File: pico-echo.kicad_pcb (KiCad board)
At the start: 2 copper layers, 22.9 x 50.8 mm, 51 parts, among them J1 USB_C_Receptacle_USB2.0, J2 I2C, J4 Conn_01x16, J5 Conn_01x12, J6 BAT, Q1 BSS83P, SW1 SW_Push, SW2 SW_Push, U1 RP2040, U2 W25Q128JVS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

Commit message: Updated tracks, not finished yet
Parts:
- D2: footprint Capacitor_SMD:C_0603_1608Metric -> LED_SMD:LED_0603_1608Metric
- moved D2 54.9 mm to (138.1, 68.2), turned to 90 degrees
- moved D4 54.3 mm to (126.0, 68.2), turned to -90 degrees
- moved C2 50.7 mm to (131.1, 90.1)
- moved R2 50.7 mm to (131.1, 91.4)
- moved C1 50.7 mm to (136.2, 90.6)
- moved Y1 50.7 mm to (133.9, 90.6)
- moved R5 50.5 mm to (126.1, 71.9)
- moved U1 50.4 mm to (132.0, 97.1)
- moved R7 50.3 mm to (130.8, 74.3), turned to -90 degrees
- moved U4 50.3 mm to (136.8, 84.0)
- moved U2 50.1 mm to (134.7, 106.8)
- moved J1 49.7 mm to (132.0, 68.6)
- moved D1 49.7 mm to (132.9, 78.2)
- moved D5 49.7 mm to (126.7, 84.0)
- moved J2 49.7 mm to (129.2, 111.9)
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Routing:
- net VBUS: track 3.72 -> 27.2 mm, vias 0 -> 2
- net Net-(D3-K): track 0.00 -> 8.36 mm
- net /QSPI_SS: track 0.00 -> 7.81 mm
- net +3V3: track 0.00 -> 6.76 mm
- net Net-(J1-CC1): track 0.00 -> 6.68 mm
- net Net-(J1-CC2): track 0.00 -> 6.21 mm
- net Net-(J1-D--PadA7): track 0.00 -> 4.70 mm
- net Net-(D2-A): track 0.00 -> 4.45 mm
- net Net-(J1-D+-PadA6): track 0.00 -> 3.71 mm
- net Net-(D1-K): track 6.73 -> 9.81 mm
- net Net-(D4-A): track 0.00 -> 2.74 mm
- net Net-(D3-A): track 0.00 -> 2.01 mm
- net Net-(U4-PROG): track 0.00 -> 1.62 mm
- net VBAT: track 4.65 -> 6.23 mm
- net Net-(U3-EN): track 0.00 -> 1.50 mm
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- added copper zone on B.Cu, net GND
- added copper zone on F.Cu, net GND
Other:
- board text added: "10"
- board text added: "11"
- board text added: "12"
- board text added: "13"
- board text added: "24"
- board text added: "25"
- board text added: "3V3"
- board text added: "5"
- board text added: "6"
- board text added: "9"
- board text added: "A0"
- board text added: "A1"
- board text added: "A2"
- board text added: "A3"
- board text added: "BAT"
- board text added: "D4"
- board text added: "EN"
- board text added: "GND"
- board text added: "M0"
- board text added: "M1"
- board text added: "RST"
- board text added: "RX"
- board text added: "SCK"
- board text added: "SCL"
- board text added: "SDA"
- board text added: "TX"
- board text added: "USB"

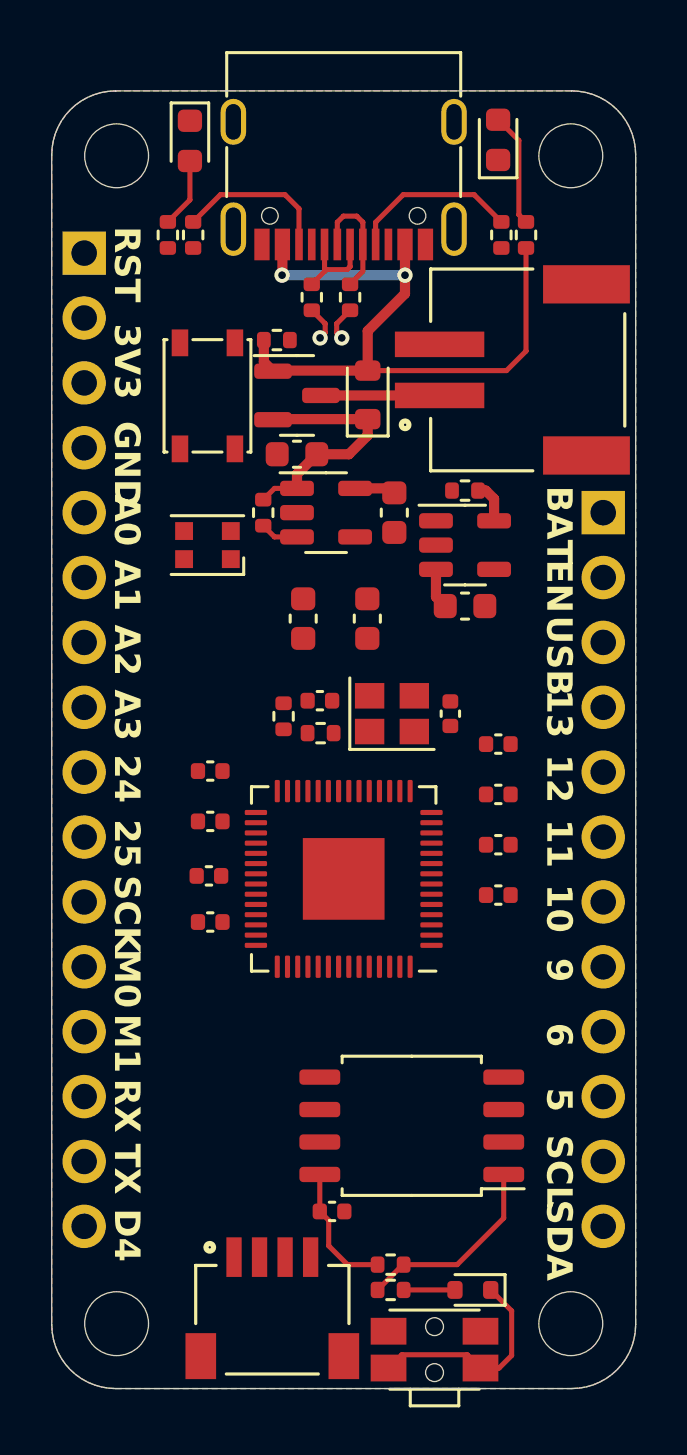
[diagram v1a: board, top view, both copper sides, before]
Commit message: Add SWD conn, change Flash to USON, tracks almost finished
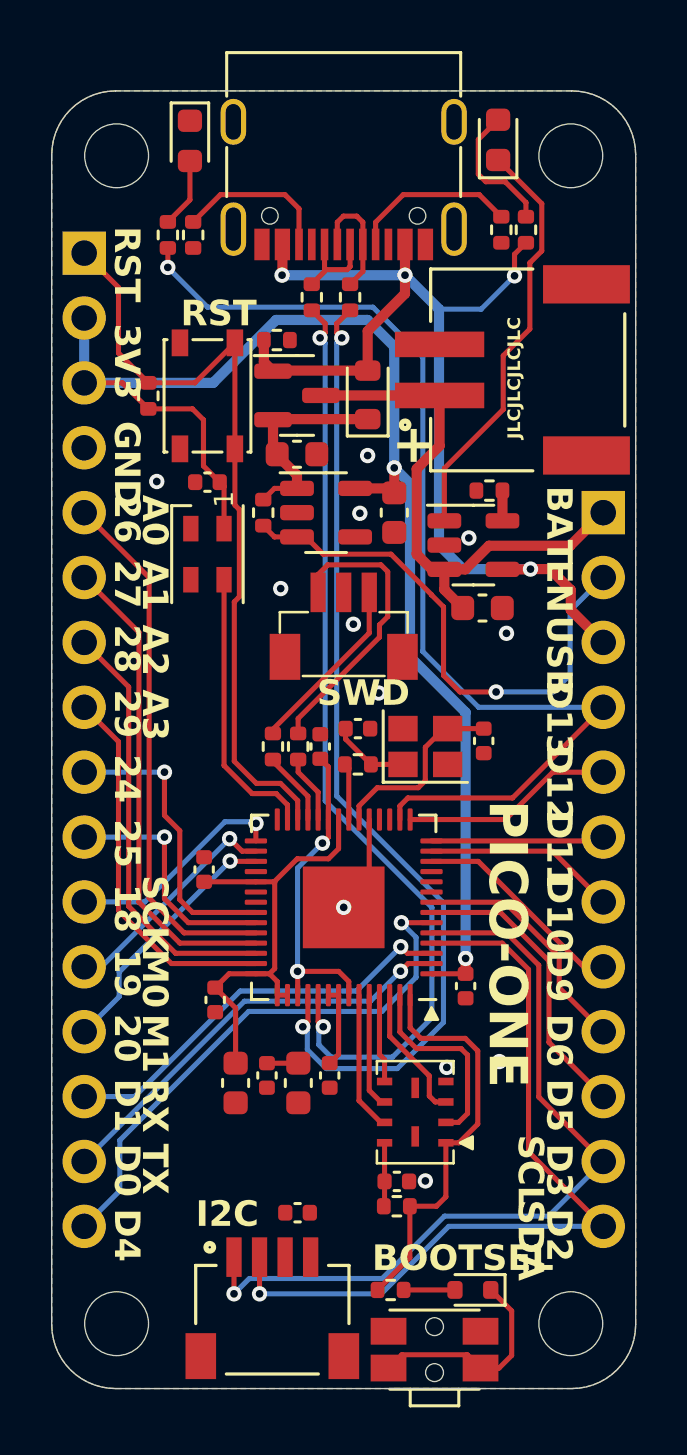
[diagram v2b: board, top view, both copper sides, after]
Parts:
- added J7: PICO Probe, BM03B-SRSS-TBT_LF__SN_:BM03BSRSSTBTLFSN, F.Cu at (132.0, 86.7)
- added R14: 100, Resistor_SMD:R_0402_1005Metric, F.Cu at (130.2, 91.9)
- added R15: 100, Resistor_SMD:R_0402_1005Metric, F.Cu at (129.2, 91.9)
- D5: footprint LED_SMD:LED_WS2812B-2020_PLCC4_2.0x2.0mm -> LED_SMD:LED_SK6805_PLCC4_2.4x2.7mm_P1.3mm
- U2: footprint Package_SO:SOIC-8_5.23x5.23mm_P1.27mm -> SPI-Flash:USON-8-3x4
- moved C9 18.4 mm to (130.2, 105.1), turned to -90 degrees
- moved C6 18.4 mm to (127.8, 105.1), turned to -90 degrees
- moved C7 15.8 mm to (129.0, 104.8), turned to -90 degrees
- moved C13 15.7 mm to (130.2, 110.2)
- moved R1 13.6 mm to (124.4, 78.2), turned to 90 degrees
- moved C12 11.3 mm to (126.7, 81.6), turned to 180 degrees
- moved C11 9.67 mm to (131.5, 104.8), turned to -90 degrees
- moved C8 7.22 mm to (131.1, 91.9), turned to 90 degrees
- moved C10 5.68 mm to (136.8, 101.3), turned to -90 degrees
- moved C15 3.06 mm to (127.0, 101.9), turned to -90 degrees
- moved C16 2.79 mm to (134.1, 109.0)
- moved R3 2.30 mm to (134.1, 109.9)
- moved R2 1.91 mm to (132.6, 92.6)
- moved C2 1.85 mm to (132.6, 91.2)
- moved Y1 1.83 mm to (135.2, 91.9)
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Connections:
- D5 pad 4: /RGB_LED -> /GPIO16
- J2 pad 1: /SCL -> /GPIO3
- J2 pad 2: /SDA -> /GPIO2
- J4 pad 10: unconnected-(J4-Pin_10-Pad10) -> /GPIO25
- J4 pad 11: unconnected-(J4-Pin_11-Pad11) -> /GPIO18
- J4 pad 12: unconnected-(J4-Pin_12-Pad12) -> /GPIO19
- J4 pad 13: unconnected-(J4-Pin_13-Pad13) -> /GPIO20
- J4 pad 14: unconnected-(J4-Pin_14-Pad14) -> /GPIO1
- J4 pad 15: unconnected-(J4-Pin_15-Pad15) -> /GPIO0
- J4 pad 16: unconnected-(J4-Pin_16-Pad16) -> /GPIO4
- J4 pad 3: GND -> +3V3
- J4 pad 4: /GPIO26_ADC0 -> GND
- J4 pad 5: /GPIO27_ADC1 -> /GPIO26_ADC0
- J4 pad 6: /GPIO28_ADC2 -> /GPIO27_ADC1
- J4 pad 7: /GPIO29_ADC3 -> /GPIO28_ADC2
- J4 pad 8: /GPIO24 -> /GPIO29_ADC3
- J4 pad 9: /GPIO25 -> /GPIO24
- J5 pad 1: unconnected-(J5-Pin_1-Pad1) -> VBAT
- J5 pad 10: unconnected-(J5-Pin_10-Pad10) -> /GPIO5
- J5 pad 11: unconnected-(J5-Pin_11-Pad11) -> /GPIO3
- J5 pad 12: unconnected-(J5-Pin_12-Pad12) -> /GPIO2
- J5 pad 2: unconnected-(J5-Pin_2-Pad2) -> /EN
- J5 pad 3: unconnected-(J5-Pin_3-Pad3) -> VBUS
- J5 pad 4: unconnected-(J5-Pin_4-Pad4) -> /GPIO13
- J5 pad 5: unconnected-(J5-Pin_5-Pad5) -> /GPIO12
- J5 pad 6: unconnected-(J5-Pin_6-Pad6) -> /GPIO11
- J5 pad 7: unconnected-(J5-Pin_7-Pad7) -> /GPIO10
- J5 pad 8: unconnected-(J5-Pin_8-Pad8) -> /GPIO9
- J5 pad 9: unconnected-(J5-Pin_9-Pad9) -> /GPIO6
- R9 pad 2: Net-(U3-EN) -> /EN
- U1 pad 19: unconnected-(U1-TESTEN-Pad19) -> GND
- U3 pad 3: Net-(U3-EN) -> /EN
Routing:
- net +3V3: track 6.76 -> 79.0 mm, vias 0 -> 2
- net /GPIO13: track 0.00 -> 41.8 mm, vias 0 -> 1
- net /USB_DN: track 1.38 -> 38.7 mm, vias 1 -> 2
- net /USB_DP: track 1.38 -> 37.2 mm, vias 1 -> 2
- net /GPIO3: track 0.00 -> 31.5 mm, vias 0 -> 1
- net /GPIO2: track 0.00 -> 31.5 mm, vias 0 -> 1
- net /~{RST}: track 0.00 -> 30.6 mm
- net /GPIO4: track 0.00 -> 21.7 mm, vias 0 -> 1
- net /EN: track 0.00 -> 20.9 mm, vias 0 -> 1
- net /GPIO26_ADC0: track 0.00 -> 20.9 mm
- net /GPIO27_ADC1: track 0.00 -> 18.8 mm
- net /GPIO0: track 0.00 -> 16.8 mm, vias 0 -> 1
- net /GPIO28_ADC2: track 0.00 -> 16.8 mm
- net Net-(D2-K): track 0.00 -> 16.4 mm
- net /GPIO1: track 0.00 -> 16.1 mm, vias 0 -> 1
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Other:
- board text added: "+"
- board text added: "18"
- board text added: "19"
- board text added: "20"
- board text added: "26"
- board text added: "27"
- board text added: "28"
- board text added: "29"
- board text added: "BOOTSEL"
- board text added: "D0"
- board text added: "D1"
- board text added: "D10"
- board text added: "D11"
- board text added: "D12"
- board text added: "D13"
- board text added: "D2"
- board text added: "D3"
- board text added: "D5"
- board text added: "D6"
- board text added: "D9"
- board text added: "I2C"
- board text added: "JLCJLCJLCJLC"
- board text added: "PICO-ONE"
- board text added: "SWD"
- board text removed: "10"
- board text removed: "11"
- board text removed: "12"
- board text removed: "13"
- board text removed: "5"
- board text removed: "6"
- board text removed: "9"

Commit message: Finished tracks
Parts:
- added C17: 1uF, Capacitor_SMD:C_0603_1608Metric, F.Cu at (130.5, 110.1)
- D1: value MBR0520 -> MBR0540; footprint Diode_SMD:D_SOD-110 -> Diode_SMD:D_SOD-123
- D3: value 1N4148WT -> NSR0320; footprint Diode_SMD:D_SOD-523 -> Diode_SMD:D_SOD-323_HandSoldering
- moved C13 14.9 mm to (137.3, 97.1)
- moved R1 3.27 mm to (126.7, 80.5), turned to 0 degrees
- moved SW2 1.18 mm to (126.1, 77.2)
- moved D1 0.59 mm to (132.7, 78.7)
- moved C6 0.57 mm to (127.4, 104.7)
- moved C11 0.55 mm to (131.0, 104.5)
- moved C9 0.54 mm to (129.8, 104.7)
- moved C7 0.52 mm to (128.6, 104.5)
- moved Q1 0.43 mm to (129.7, 78.2)
- moved R8 0.43 mm to (129.0, 76.0)
- moved D3 0.28 mm to (137.1, 112.9)
- moved R12 0.28 mm to (133.8, 112.9)
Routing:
- net +3V3: track 79.0 -> 135.2 mm, vias 2 -> 6
- net /GPIO2: track 31.5 -> 34.1 mm
- net +1V2: track 13.8 -> 16.3 mm
- net /~{RST}: track 30.6 -> 28.2 mm
- net /GPIO3: track 31.5 -> 33.1 mm
- net /GPIO9: track 8.43 -> 9.59 mm
- net Net-(D1-K): track 8.29 -> 9.09 mm
- net Net-(D3-A): track 2.01 -> 1.46 mm
- net GND: vias 12 -> 34
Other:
- board text added: "MI"
- board text removed: "M1"

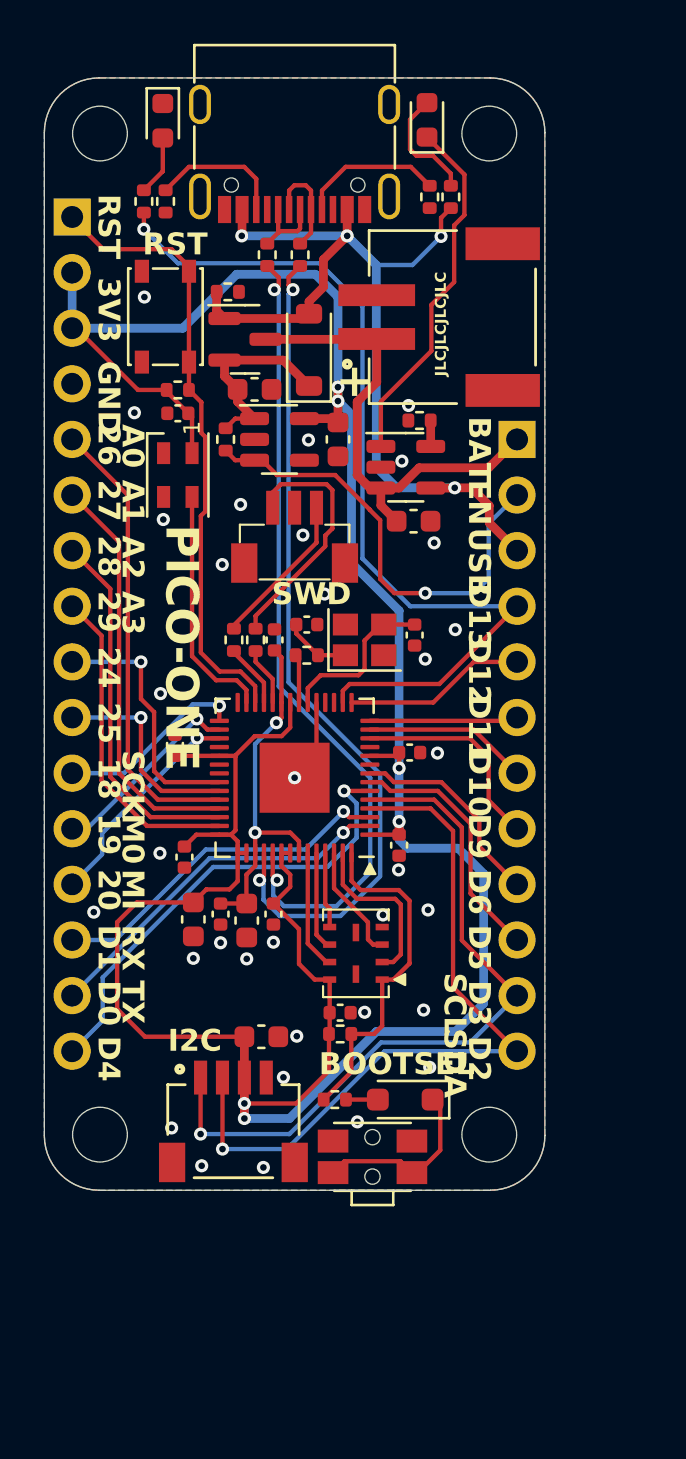
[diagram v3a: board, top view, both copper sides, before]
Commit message: Added github repo qrcode logo
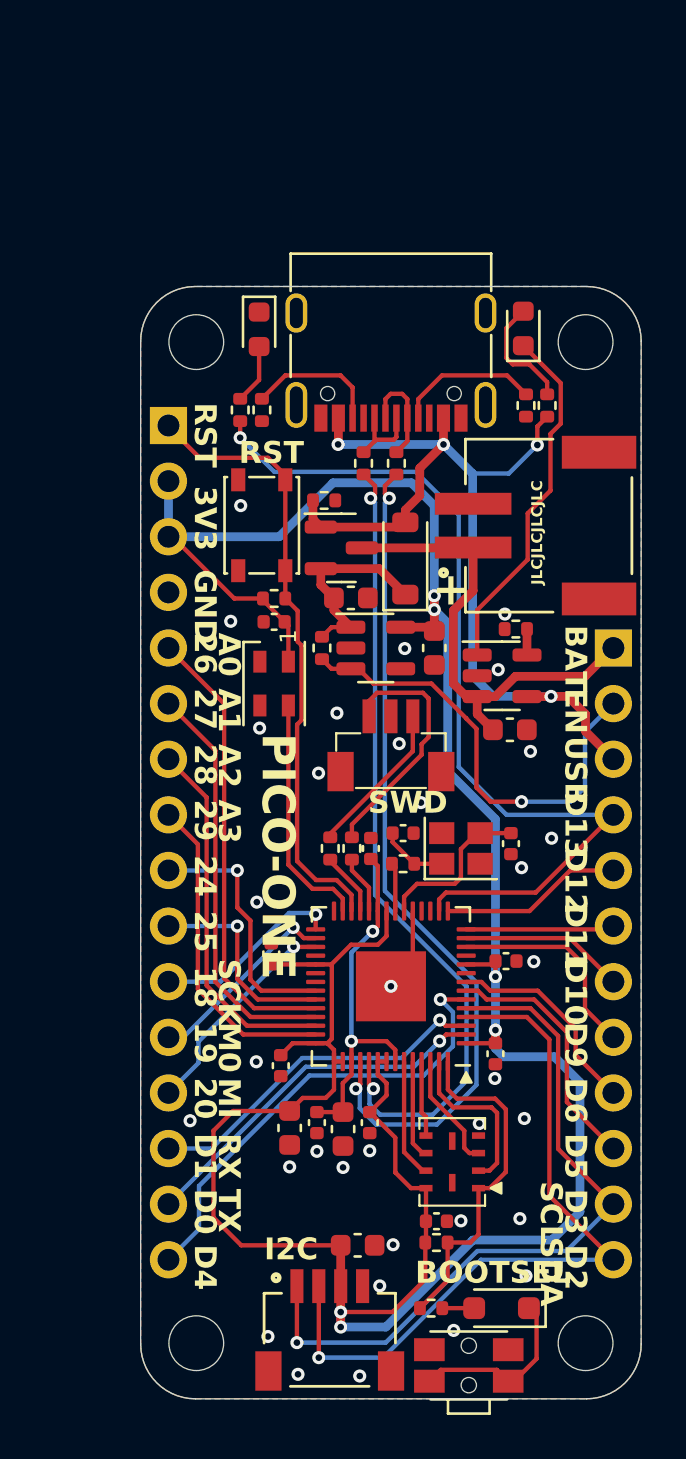
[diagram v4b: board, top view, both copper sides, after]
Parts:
- added G***: LOGO, lib:qrcode, B.Cu at (136.4, 101.2)
- moved C12 10.5 mm to (131.1, 91.1)
- moved C15 10.5 mm to (131.4, 111.4)
- moved R1 10.5 mm to (131.1, 90.0)
- moved C10 10.5 mm to (141.2, 110.8)
- moved C11 10.5 mm to (135.4, 114.0)
- moved C13 10.5 mm to (141.7, 106.6)
- moved C14 10.5 mm to (130.9, 106.3)
- moved C16 10.5 mm to (138.5, 118.5)
- moved C17 10.5 mm to (134.9, 119.6)
- moved C3 10.5 mm to (134.6, 90.0)
- moved C4 10.5 mm to (138.4, 92.3)
- moved C5 10.5 mm to (141.8, 96.0)
- moved C7 10.5 mm to (133.0, 114.0)
- moved C9 10.5 mm to (134.2, 114.3)
- moved D1 10.5 mm to (137.1, 88.2)
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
